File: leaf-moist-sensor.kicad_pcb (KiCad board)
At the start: 2 copper layers, 61 x 61 mm, 2 parts, among them P1 CONN_01X02

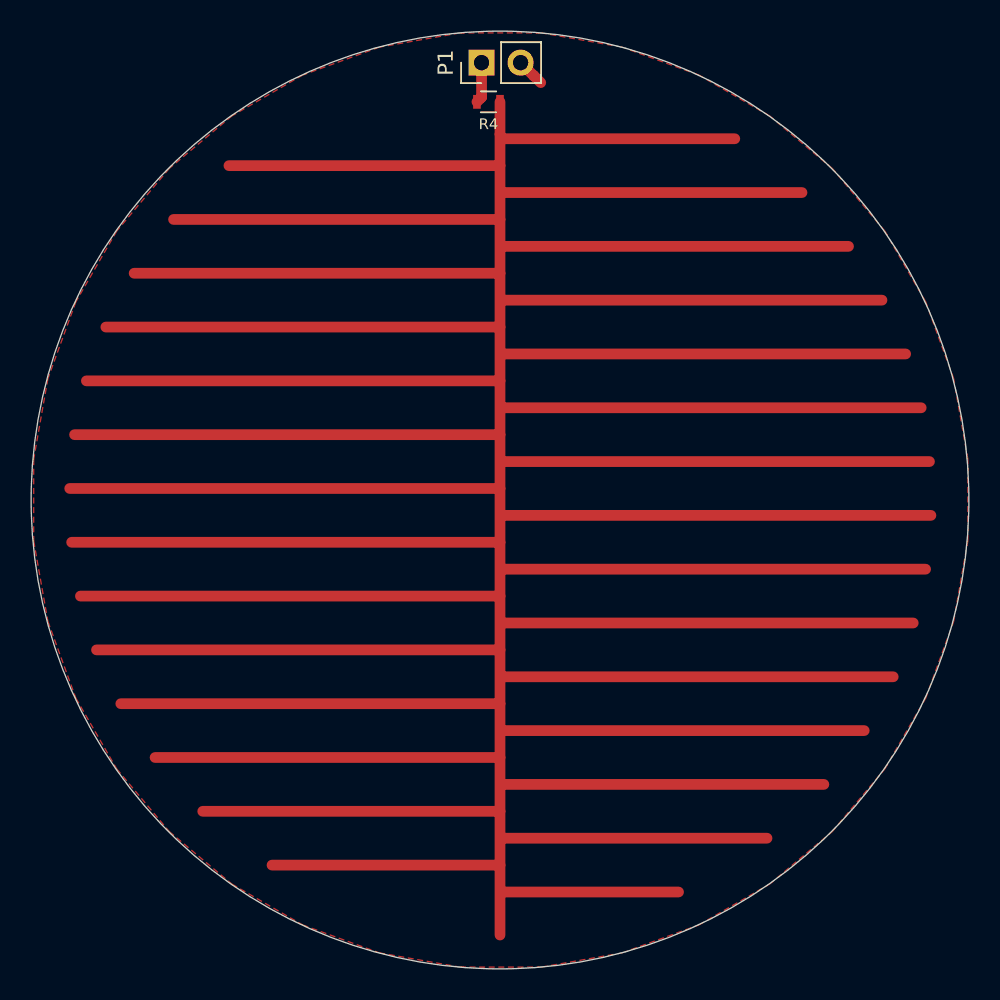
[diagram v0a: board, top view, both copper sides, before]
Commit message: 0.7mm tracks and GNDs
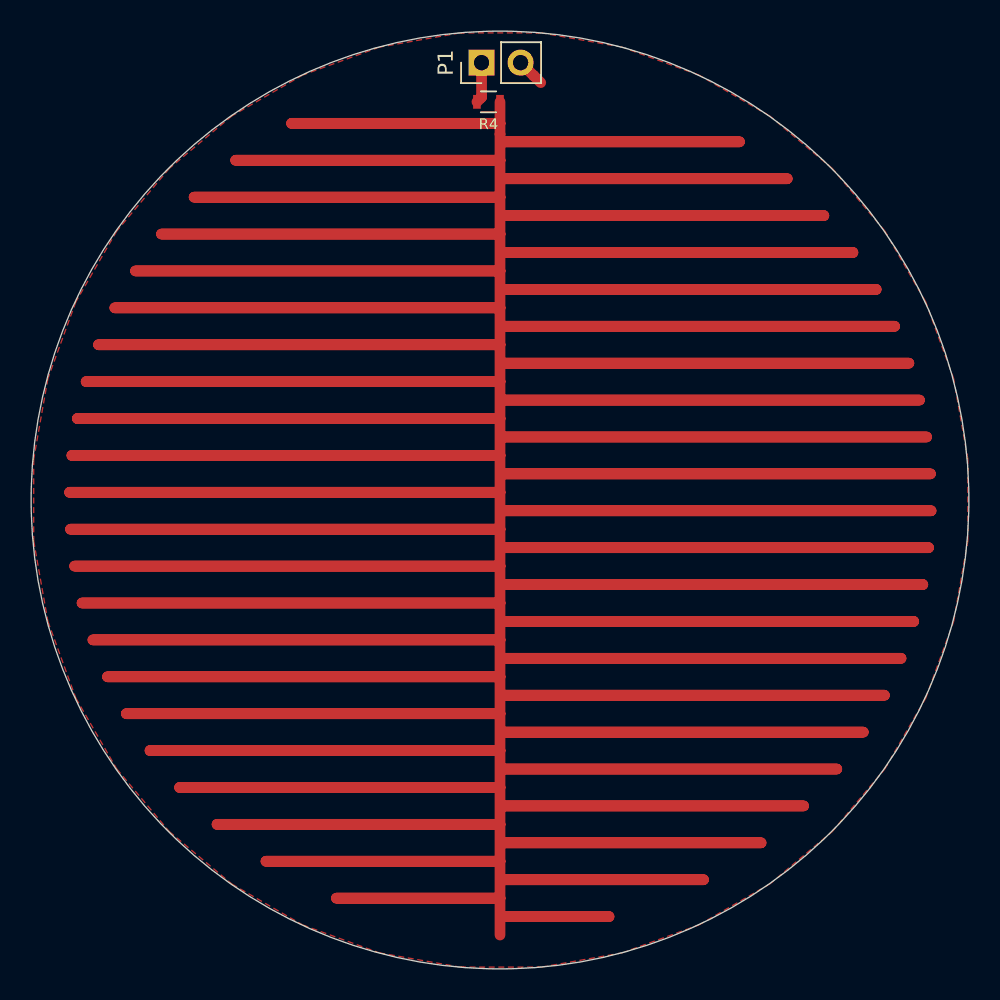
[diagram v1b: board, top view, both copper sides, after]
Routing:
- net /SENSOR_TRACK: track 733.1 -> 2065.7 mm
